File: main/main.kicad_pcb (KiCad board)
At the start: 2 copper layers, 100 x 100 mm, 9 parts

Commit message: started layout to see if practical
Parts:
- removed FID1, FID2, FID3: Fiducial, Fiducial:Fiducial_1mm_Dia_2mm_Outer
- removed G1: DOW, william_logos:dow_logo_10mm
- removed G2: MEC, william_logos:mec_small
- added BT1: RTC battery, william_batteries:Keystone_3034_1x20mm-CoinCell, F.Cu at (117.1, 168.4)
- added C1: 100N, Capacitor_SMD:C_0603_1608Metric, F.Cu at (118.8, 188.2)
- added C10: 100N, Capacitor_SMD:C_0603_1608Metric, F.Cu at (310.5, 116.6)
- added C100: 100N, Capacitor_SMD:C_0603_1608Metric, F.Cu at (310.9, 109.1)
- added C101: 100N, Capacitor_SMD:C_0603_1608Metric, F.Cu at (299.3, 147.0)
- added C102: 100N, Capacitor_SMD:C_0603_1608Metric, F.Cu at (299.3, 142.0)
- added C103: 100N, Capacitor_SMD:C_0603_1608Metric, F.Cu at (319.0, 132.2)
- added C104: 100N, Capacitor_SMD:C_0603_1608Metric, F.Cu at (327.9, 113.4)
- added C105: 100N, Capacitor_SMD:C_0603_1608Metric, F.Cu at (302.7, 171.1)
- added C106: 100N, Capacitor_SMD:C_0603_1608Metric, F.Cu at (273.4, 175.7)
- added C107: 100N, Capacitor_SMD:C_0603_1608Metric, F.Cu at (323.0, 129.7)
- added C108: 100N, Capacitor_SMD:C_0603_1608Metric, F.Cu at (249.4, 175.7)
- added C109: 100N, Capacitor_SMD:C_0603_1608Metric, F.Cu at (323.4, 124.6)
- added C11: 100N, Capacitor_SMD:C_0603_1608Metric, F.Cu at (309.2, 135.8)
- added C110: 100N, Capacitor_SMD:C_0603_1608Metric, F.Cu at (225.3, 175.7)
- added C111: 100N, Capacitor_SMD:C_0603_1608Metric, F.Cu at (233.3, 175.7)
- added C112: 100N, Capacitor_SMD:C_0603_1608Metric, F.Cu at (245.3, 175.7)
- added C113: 100N, Capacitor_SMD:C_0603_1608Metric, F.Cu at (253.4, 175.7)
- added C114: 100N, Capacitor_SMD:C_0603_1608Metric, F.Cu at (261.4, 175.7)
- added C115: 4U7, Capacitor_SMD:C_0603_1608Metric, F.Cu at (325.8, 74.3)
- added C116: 100N, Capacitor_SMD:C_0603_1608Metric, F.Cu at (325.8, 71.8)
- added C117: 100N, Capacitor_SMD:C_0603_1608Metric, F.Cu at (321.8, 74.3)
- added C118: 10N, Capacitor_SMD:C_0603_1608Metric, F.Cu at (317.8, 71.8)
- added C119: 2U2, Capacitor_SMD:C_0603_1608Metric, F.Cu at (326.9, 62.3)
- added C12: 100N, Capacitor_SMD:C_0603_1608Metric, F.Cu at (328.2, 152.0)
- added C120: 100N, Capacitor_SMD:C_0603_1608Metric, F.Cu at (317.8, 74.3)
- added C121: 100N, Capacitor_SMD:C_0603_1608Metric, F.Cu at (326.9, 64.8)
- added C122: 100N, Capacitor_SMD:C_0603_1608Metric, F.Cu at (321.8, 71.8)
- added C123: 100N, Capacitor_SMD:C_0603_1608Metric, F.Cu at (326.9, 67.3)
- added C13: 100N, Capacitor_SMD:C_0603_1608Metric, F.Cu at (313.3, 133.3)
- added C14: 100N, Capacitor_SMD:C_0603_1608Metric, F.Cu at (313.3, 138.3)
- added C15: 100N, Capacitor_SMD:C_0603_1608Metric, F.Cu at (309.2, 130.8)
- added C16: 100N, Capacitor_SMD:C_0603_1608Metric, F.Cu at (302.7, 173.6)
- added C17: 100N, Capacitor_SMD:C_0603_1608Metric, F.Cu at (288.5, 170.6)
- added C18: 100N, Capacitor_SMD:C_0603_1608Metric, F.Cu at (314.9, 109.1)
- added C19: 100N, Capacitor_SMD:C_0603_1608Metric, F.Cu at (269.4, 175.7)
- added C2: 10N, Capacitor_SMD:C_0603_1608Metric, F.Cu at (114.7, 188.2)
- added C20: 100N, Capacitor_SMD:C_0603_1608Metric, F.Cu at (293.7, 175.7)
- added C21: 100N, Capacitor_SMD:C_0603_1608Metric, F.Cu at (221.3, 175.7)
- added C22: 100N, Capacitor_SMD:C_0603_1608Metric, F.Cu at (327.5, 126.0)
- added C23: 100N, Capacitor_SMD:C_0603_1608Metric, F.Cu at (313.3, 130.8)
- added C24: 100N, Capacitor_SMD:C_0603_1608Metric, F.Cu at (323.0, 132.2)
- added C25: 100N, Capacitor_SMD:C_0603_1608Metric, F.Cu at (292.5, 173.1)
- added C26: 100N, Capacitor_SMD:C_0603_1608Metric, F.Cu at (314.5, 116.6)
- added C27: 100N, Capacitor_SMD:C_0603_1608Metric, F.Cu at (327.9, 118.5)
- added C28: 100N, Capacitor_SMD:C_0603_1608Metric, F.Cu at (298.9, 152.1)
- added C29: 100N, Capacitor_SMD:C_0603_1608Metric, F.Cu at (295.3, 142.0)
- added C3: 100N, Capacitor_SMD:C_0603_1608Metric, F.Cu at (106.7, 188.2)
- added C30: 100N, Capacitor_SMD:C_0603_1608Metric, F.Cu at (312.9, 143.3)
- added C31: 100N, Capacitor_SMD:C_0603_1608Metric, F.Cu at (301.5, 168.6)
- added C32: 100N, Capacitor_SMD:C_0603_1608Metric, F.Cu at (308.8, 146.5)
- added C33: 100N, Capacitor_SMD:C_0603_1608Metric, F.Cu at (265.4, 175.7)
- added C34: 100N, Capacitor_SMD:C_0603_1608Metric, F.Cu at (310.5, 119.1)
- added C35: 100N, Capacitor_SMD:C_0603_1608Metric, F.Cu at (323.4, 122.1)
- added C36: 100N, Capacitor_SMD:C_0603_1608Metric, F.Cu at (294.5, 157.1)
- added C37: 100N, Capacitor_SMD:C_0603_1608Metric, F.Cu at (289.7, 175.7)
- added C38: 100N, Capacitor_SMD:C_0603_1608Metric, F.Cu at (324.2, 157.0)
- added C39: 100N, Capacitor_SMD:C_0603_1608Metric, F.Cu at (309.2, 133.3)
- added C4: 10U, Capacitor_SMD:C_0603_1608Metric, F.Cu at (110.7, 188.2)
- added C40: 100N, Capacitor_SMD:C_0603_1608Metric, F.Cu at (319.0, 134.7)
- added C41: 100N, Capacitor_SMD:C_0603_1608Metric, F.Cu at (325.0, 162.0)
- added C42: 100N, Capacitor_SMD:C_0603_1608Metric, F.Cu at (301.9, 163.6)
- added C43: 100N, Capacitor_SMD:C_0603_1608Metric, F.Cu at (314.5, 119.1)
- added C44: 100N, Capacitor_SMD:C_0603_1608Metric, F.Cu at (327.9, 115.9)
- added C45: 100N, Capacitor_SMD:C_0603_1608Metric, F.Cu at (310.5, 121.7)
- added C46: 100N, Capacitor_SMD:C_0603_1608Metric, F.Cu at (288.5, 173.1)
- added C47: 100N, Capacitor_SMD:C_0603_1608Metric, F.Cu at (308.8, 149.0)
- added C48: 100N, Capacitor_SMD:C_0603_1608Metric, F.Cu at (277.4, 175.7)
- added C49: 100N, Capacitor_SMD:C_0603_1608Metric, F.Cu at (327.9, 110.9)
- added C5: 100N, Capacitor_SMD:C_0603_1608Metric, F.Cu at (237.3, 175.7)
- added C50: 100N, Capacitor_SMD:C_0603_1608Metric, F.Cu at (309.2, 138.3)
- added C51: 100N, Capacitor_SMD:C_0603_1608Metric, F.Cu at (328.6, 149.5)
- added C52: 100N, Capacitor_SMD:C_0603_1608Metric, F.Cu at (314.9, 111.6)
- added C53: 100N, Capacitor_SMD:C_0603_1608Metric, F.Cu at (319.0, 129.7)
- added C54: 100N, Capacitor_SMD:C_0603_1608Metric, F.Cu at (328.6, 146.9)
- added C55: 100N, Capacitor_SMD:C_0603_1608Metric, F.Cu at (294.9, 152.1)
- added C56: 100N, Capacitor_SMD:C_0603_1608Metric, F.Cu at (323.4, 127.2)
- added C57: 100N, Capacitor_SMD:C_0603_1608Metric, F.Cu at (295.3, 147.0)
- added C58: 100N, Capacitor_SMD:C_0603_1608Metric, F.Cu at (310.9, 114.1)
- added C59: 100N, Capacitor_SMD:C_0603_1608Metric, F.Cu at (305.5, 168.6)
- added C6: 100N, Capacitor_SMD:C_0603_1608Metric, F.Cu at (229.3, 175.7)
- added C60: 100N, Capacitor_SMD:C_0603_1608Metric, F.Cu at (293.7, 178.2)
- added C61: 100N, Capacitor_SMD:C_0603_1608Metric, F.Cu at (308.8, 144.0)
- added C62: 100N, Capacitor_SMD:C_0603_1608Metric, F.Cu at (309.2, 140.8)
- added C63: 100N, Capacitor_SMD:C_0603_1608Metric, F.Cu at (324.2, 154.5)
- added C64: 100N, Capacitor_SMD:C_0603_1608Metric, F.Cu at (313.3, 135.8)
- added C65: 100N, Capacitor_SMD:C_0603_1608Metric, F.Cu at (294.9, 149.5)
- added C66: 100N, Capacitor_SMD:C_0603_1608Metric, F.Cu at (324.2, 152.0)
- added C67: 100N, Capacitor_SMD:C_0603_1608Metric, F.Cu at (327.9, 123.5)
- added C68: 100N, Capacitor_SMD:C_0603_1608Metric, F.Cu at (305.9, 166.1)
- added C69: 100N, Capacitor_SMD:C_0603_1608Metric, F.Cu at (299.3, 144.5)
- added C7: 100N, Capacitor_SMD:C_0603_1608Metric, F.Cu at (301.9, 161.1)
- added C70: 100N, Capacitor_SMD:C_0603_1608Metric, F.Cu at (319.0, 139.7)
- added C71: 100N, Capacitor_SMD:C_0603_1608Metric, F.Cu at (327.5, 131.0)
- added C72: 100N, Capacitor_SMD:C_0603_1608Metric, F.Cu at (312.9, 145.8)
- added C73: 100N, Capacitor_SMD:C_0603_1608Metric, F.Cu at (305.9, 161.1)
- added C74: 100N, Capacitor_SMD:C_0603_1608Metric, F.Cu at (325.0, 159.5)
- added C75: 100N, Capacitor_SMD:C_0603_1608Metric, F.Cu at (324.6, 144.4)
- added C76: 100N, Capacitor_SMD:C_0603_1608Metric, F.Cu at (328.2, 157.0)
- added C77: 100N, Capacitor_SMD:C_0603_1608Metric, F.Cu at (292.5, 170.6)
- added C78: 100N, Capacitor_SMD:C_0603_1608Metric, F.Cu at (298.9, 149.5)
- added C79: 100N, Capacitor_SMD:C_0603_1608Metric, F.Cu at (319.4, 122.1)
- added C8: 100N, Capacitor_SMD:C_0603_1608Metric, F.Cu at (257.4, 175.7)
- added C80: 100N, Capacitor_SMD:C_0603_1608Metric, F.Cu at (310.9, 111.6)
- added C81: 100N, Capacitor_SMD:C_0603_1608Metric, F.Cu at (294.9, 154.6)
- added C82: 100N, Capacitor_SMD:C_0603_1608Metric, F.Cu at (327.9, 121.0)
- added C83: 100N, Capacitor_SMD:C_0603_1608Metric, F.Cu at (328.2, 154.5)
- added C84: 100N, Capacitor_SMD:C_0603_1608Metric, F.Cu at (319.4, 127.2)
- added C85: 100N, Capacitor_SMD:C_0603_1608Metric, F.Cu at (306.7, 171.1)
- added C86: 100N, Capacitor_SMD:C_0603_1608Metric, F.Cu at (289.7, 178.2)
- added C87: 100N, Capacitor_SMD:C_0603_1608Metric, F.Cu at (327.5, 128.5)
- added C88: 100N, Capacitor_SMD:C_0603_1608Metric, F.Cu at (328.6, 144.4)
- added C89: 100N, Capacitor_SMD:C_0603_1608Metric, F.Cu at (314.9, 114.1)
- added C9: 100N, Capacitor_SMD:C_0603_1608Metric, F.Cu at (241.3, 175.7)
- added C90: 100N, Capacitor_SMD:C_0603_1608Metric, F.Cu at (295.3, 144.5)
- added C91: 100N, Capacitor_SMD:C_0603_1608Metric, F.Cu at (305.9, 163.6)
- added C92: 100N, Capacitor_SMD:C_0603_1608Metric, F.Cu at (324.6, 149.5)
- added C93: 100N, Capacitor_SMD:C_0603_1608Metric, F.Cu at (323.0, 134.7)
- added C94: 100N, Capacitor_SMD:C_0603_1608Metric, F.Cu at (319.4, 124.6)
- added C95: 100N, Capacitor_SMD:C_0603_1608Metric, F.Cu at (319.0, 137.2)
- added C96: 100N, Capacitor_SMD:C_0603_1608Metric, F.Cu at (324.6, 146.9)
- added C97: 100N, Capacitor_SMD:C_0603_1608Metric, F.Cu at (313.3, 140.8)
- added C98: 100N, Capacitor_SMD:C_0603_1608Metric, F.Cu at (301.9, 166.1)
- added C99: 100N, Capacitor_SMD:C_0603_1608Metric, F.Cu at (306.7, 173.6)
- added D1: WS2813-Mini, william_led:WS2813-Mini-3.5mm_x_3.5mm, F.Cu at (8.96, 5.14)
- added D10: WS2813-Mini, william_led:WS2813-Mini-3.5mm_x_3.5mm, F.Cu at (8.58, 85.2)
- added D100: WS2813-Mini, william_led:WS2813-Mini-3.5mm_x_3.5mm, F.Cu at (82.5, 95.3)
- added D101: WS2813-Mini, william_led:WS2813-Mini-3.5mm_x_3.5mm, F.Cu at (85.7, 5.14)
- added D102: WS2813-Mini, william_led:WS2813-Mini-3.5mm_x_3.5mm, F.Cu at (94.0, 12.8)
- added D103: WS2813-Mini, william_led:WS2813-Mini-3.5mm_x_3.5mm, F.Cu at (93.0, 23.6)
- added D104: WS2813-Mini, william_led:WS2813-Mini-3.5mm_x_3.5mm, F.Cu at (94.4, 31.6)
- added D105: WS2813-Mini, william_led:WS2813-Mini-3.5mm_x_3.5mm, F.Cu at (93.4, 41.0)
- added D106: WS2813-Mini, william_led:WS2813-Mini-3.5mm_x_3.5mm, F.Cu at (92.8, 48.2)
- added D107: WS2813-Mini, william_led:WS2813-Mini-3.5mm_x_3.5mm, F.Cu at (93.3, 59.6)
- added D108: WS2813-Mini, william_led:WS2813-Mini-3.5mm_x_3.5mm, F.Cu at (93.7, 68.5)
- added D109: WS2813-Mini, william_led:WS2813-Mini-3.5mm_x_3.5mm, F.Cu at (90.5, 86.0)
- added D11: WS2813-Mini, william_led:WS2813-Mini-3.5mm_x_3.5mm, F.Cu at (16.6, 5.14)
- added D110: WS2813-Mini, william_led:WS2813-Mini-3.5mm_x_3.5mm, F.Cu at (90.7, 95.1)
- added D12: WS2813-Mini, william_led:WS2813-Mini-3.5mm_x_3.5mm, F.Cu at (17.8, 12.4)
- added D13: WS2813-Mini, william_led:WS2813-Mini-3.5mm_x_3.5mm, F.Cu at (16.6, 21.9)
- added D14: WS2813-Mini, william_led:WS2813-Mini-3.5mm_x_3.5mm, F.Cu at (16.5, 31.4)
- added D15: WS2813-Mini, william_led:WS2813-Mini-3.5mm_x_3.5mm, F.Cu at (16.4, 39.1)
- added D16: WS2813-Mini, william_led:WS2813-Mini-3.5mm_x_3.5mm, F.Cu at (17.3, 47.1)
- added D17: WS2813-Mini, william_led:WS2813-Mini-3.5mm_x_3.5mm, F.Cu at (17.7, 55.8)
- added D18: WS2813-Mini, william_led:WS2813-Mini-3.5mm_x_3.5mm, F.Cu at (18.2, 74.4)
- added D19: WS2813-Mini, william_led:WS2813-Mini-3.5mm_x_3.5mm, F.Cu at (15.4, 85.7)
- added D2: WS2813-Mini, william_led:WS2813-Mini-3.5mm_x_3.5mm, F.Cu at (8.96, 12.5)
- added D20: WS2813-Mini, william_led:WS2813-Mini-3.5mm_x_3.5mm, F.Cu at (15.6, 95.2)
- added D21: WS2813-Mini, william_led:WS2813-Mini-3.5mm_x_3.5mm, F.Cu at (24.3, 5.14)
- added D22: WS2813-Mini, william_led:WS2813-Mini-3.5mm_x_3.5mm, F.Cu at (26.1, 12.1)
- added D23: WS2813-Mini, william_led:WS2813-Mini-3.5mm_x_3.5mm, F.Cu at (24.8, 22.2)
- added D24: WS2813-Mini, william_led:WS2813-Mini-3.5mm_x_3.5mm, F.Cu at (25.2, 31.4)
- added D25: WS2813-Mini, william_led:WS2813-Mini-3.5mm_x_3.5mm, F.Cu at (26.2, 39.1)
- added D26: WS2813-Mini, william_led:WS2813-Mini-3.5mm_x_3.5mm, F.Cu at (27.1, 46.8)
- added D27: WS2813-Mini, william_led:WS2813-Mini-3.5mm_x_3.5mm, F.Cu at (26.5, 55.6)
- added D28: WS2813-Mini, william_led:WS2813-Mini-3.5mm_x_3.5mm, F.Cu at (27.1, 74.4)
- added D29: WS2813-Mini, william_led:WS2813-Mini-3.5mm_x_3.5mm, F.Cu at (24.3, 85.4)
- added D3: WS2813-Mini, william_led:WS2813-Mini-3.5mm_x_3.5mm, F.Cu at (8.96, 22.0)
- added D30: WS2813-Mini, william_led:WS2813-Mini-3.5mm_x_3.5mm, F.Cu at (26.5, 94.9)
- added D31: WS2813-Mini, william_led:WS2813-Mini-3.5mm_x_3.5mm, F.Cu at (32.0, 5.14)
- added D32: WS2813-Mini, william_led:WS2813-Mini-3.5mm_x_3.5mm, F.Cu at (34.9, 12.1)
- added D33: WS2813-Mini, william_led:WS2813-Mini-3.5mm_x_3.5mm, F.Cu at (36.8, 22.4)
- added D34: WS2813-Mini, william_led:WS2813-Mini-3.5mm_x_3.5mm, F.Cu at (33.8, 31.4)
- added D35: WS2813-Mini, william_led:WS2813-Mini-3.5mm_x_3.5mm, F.Cu at (36.0, 40.1)
- added D36: WS2813-Mini, william_led:WS2813-Mini-3.5mm_x_3.5mm, F.Cu at (35.9, 46.9)
- added D37: WS2813-Mini, william_led:WS2813-Mini-3.5mm_x_3.5mm, F.Cu at (34.2, 56.1)
- added D38: WS2813-Mini, william_led:WS2813-Mini-3.5mm_x_3.5mm, F.Cu at (36.3, 74.9)
- added D39: WS2813-Mini, william_led:WS2813-Mini-3.5mm_x_3.5mm, F.Cu at (34.5, 85.3)
- added D4: WS2813-Mini, william_led:WS2813-Mini-3.5mm_x_3.5mm, F.Cu at (8.96, 31.4)
- added D40: WS2813-Mini, william_led:WS2813-Mini-3.5mm_x_3.5mm, F.Cu at (34.4, 95.3)
- added D41: WS2813-Mini, william_led:WS2813-Mini-3.5mm_x_3.5mm, F.Cu at (39.6, 5.14)
- added D42: WS2813-Mini, william_led:WS2813-Mini-3.5mm_x_3.5mm, F.Cu at (46.9, 11.9)
- added D43: WS2813-Mini, william_led:WS2813-Mini-3.5mm_x_3.5mm, F.Cu at (45.5, 22.4)
- added D44: WS2813-Mini, william_led:WS2813-Mini-3.5mm_x_3.5mm, F.Cu at (42.5, 31.4)
- added D45: WS2813-Mini, william_led:WS2813-Mini-3.5mm_x_3.5mm, F.Cu at (44.8, 39.2)
- added D46: WS2813-Mini, william_led:WS2813-Mini-3.5mm_x_3.5mm, F.Cu at (45.3, 45.5)
- added D47: WS2813-Mini, william_led:WS2813-Mini-3.5mm_x_3.5mm, F.Cu at (43.0, 58.0)
- added D48: WS2813-Mini, william_led:WS2813-Mini-3.5mm_x_3.5mm, F.Cu at (45.4, 75.1)
- added D49: WS2813-Mini, william_led:WS2813-Mini-3.5mm_x_3.5mm, F.Cu at (45.5, 85.0)
- added D5: WS2813-Mini, william_led:WS2813-Mini-3.5mm_x_3.5mm, F.Cu at (8.96, 38.9)
- added D50: WS2813-Mini, william_led:WS2813-Mini-3.5mm_x_3.5mm, F.Cu at (43.2, 95.4)
- added D51: WS2813-Mini, william_led:WS2813-Mini-3.5mm_x_3.5mm, F.Cu at (47.3, 5.14)
- added D52: WS2813-Mini, william_led:WS2813-Mini-3.5mm_x_3.5mm, F.Cu at (57.3, 11.4)
- added D53: WS2813-Mini, william_led:WS2813-Mini-3.5mm_x_3.5mm, F.Cu at (52.8, 22.4)
- added D54: WS2813-Mini, william_led:WS2813-Mini-3.5mm_x_3.5mm, F.Cu at (51.2, 31.4)
- added D55: WS2813-Mini, william_led:WS2813-Mini-3.5mm_x_3.5mm, F.Cu at (53.0, 38.2)
- added D56: WS2813-Mini, william_led:WS2813-Mini-3.5mm_x_3.5mm, F.Cu at (53.8, 45.0)
- added D57: WS2813-Mini, william_led:WS2813-Mini-3.5mm_x_3.5mm, F.Cu at (50.7, 58.2)
- added D58: WS2813-Mini, william_led:WS2813-Mini-3.5mm_x_3.5mm, F.Cu at (54.0, 75.1)
- added D59: WS2813-Mini, william_led:WS2813-Mini-3.5mm_x_3.5mm, F.Cu at (53.7, 84.9)
- added D6: WS2813-Mini, william_led:WS2813-Mini-3.5mm_x_3.5mm, F.Cu at (8.96, 47.3)
- added D60: WS2813-Mini, william_led:WS2813-Mini-3.5mm_x_3.5mm, F.Cu at (51.4, 95.7)
- added D61: WS2813-Mini, william_led:WS2813-Mini-3.5mm_x_3.5mm, F.Cu at (55.0, 5.14)
- added D62: WS2813-Mini, william_led:WS2813-Mini-3.5mm_x_3.5mm, F.Cu at (66.4, 11.5)
- added D63: WS2813-Mini, william_led:WS2813-Mini-3.5mm_x_3.5mm, F.Cu at (59.5, 23.4)
- added D64: WS2813-Mini, william_led:WS2813-Mini-3.5mm_x_3.5mm, F.Cu at (59.9, 31.4)
- added D65: WS2813-Mini, william_led:WS2813-Mini-3.5mm_x_3.5mm, F.Cu at (62.6, 39.1)
- added D66: WS2813-Mini, william_led:WS2813-Mini-3.5mm_x_3.5mm, F.Cu at (62.9, 47.7)
- added D67: WS2813-Mini, william_led:WS2813-Mini-3.5mm_x_3.5mm, F.Cu at (58.6, 58.0)
- added D68: WS2813-Mini, william_led:WS2813-Mini-3.5mm_x_3.5mm, F.Cu at (62.8, 72.6)
- added D69: WS2813-Mini, william_led:WS2813-Mini-3.5mm_x_3.5mm, F.Cu at (59.9, 84.5)
- added D7: WS2813-Mini, william_led:WS2813-Mini-3.5mm_x_3.5mm, F.Cu at (8.96, 55.1)
- added D70: WS2813-Mini, william_led:WS2813-Mini-3.5mm_x_3.5mm, F.Cu at (59.6, 95.8)
- added D71: WS2813-Mini, william_led:WS2813-Mini-3.5mm_x_3.5mm, F.Cu at (62.7, 5.14)
- added D72: WS2813-Mini, william_led:WS2813-Mini-3.5mm_x_3.5mm, F.Cu at (73.1, 11.9)
- added D73: WS2813-Mini, william_led:WS2813-Mini-3.5mm_x_3.5mm, F.Cu at (67.8, 23.3)
- added D74: WS2813-Mini, william_led:WS2813-Mini-3.5mm_x_3.5mm, F.Cu at (68.5, 31.4)
- added D75: WS2813-Mini, william_led:WS2813-Mini-3.5mm_x_3.5mm, F.Cu at (69.0, 38.8)
- added D76: WS2813-Mini, william_led:WS2813-Mini-3.5mm_x_3.5mm, F.Cu at (70.8, 45.0)
- added D77: WS2813-Mini, william_led:WS2813-Mini-3.5mm_x_3.5mm, F.Cu at (66.9, 58.4)
- added D78: WS2813-Mini, william_led:WS2813-Mini-3.5mm_x_3.5mm, F.Cu at (72.8, 67.9)
- added D79: WS2813-Mini, william_led:WS2813-Mini-3.5mm_x_3.5mm, F.Cu at (66.5, 85.5)
- added D8: WS2813-Mini, william_led:WS2813-Mini-3.5mm_x_3.5mm, F.Cu at (8.58, 63.1)
- added D80: WS2813-Mini, william_led:WS2813-Mini-3.5mm_x_3.5mm, F.Cu at (67.8, 95.4)
- added D81: WS2813-Mini, william_led:WS2813-Mini-3.5mm_x_3.5mm, F.Cu at (70.3, 5.14)
- added D82: WS2813-Mini, william_led:WS2813-Mini-3.5mm_x_3.5mm, F.Cu at (78.3, 12.6)
- added D83: WS2813-Mini, william_led:WS2813-Mini-3.5mm_x_3.5mm, F.Cu at (75.0, 23.7)
- added D84: WS2813-Mini, william_led:WS2813-Mini-3.5mm_x_3.5mm, F.Cu at (77.2, 31.4)
- added D85: WS2813-Mini, william_led:WS2813-Mini-3.5mm_x_3.5mm, F.Cu at (74.9, 39.9)
- added D86: WS2813-Mini, william_led:WS2813-Mini-3.5mm_x_3.5mm, F.Cu at (76.3, 48.4)
- added D87: WS2813-Mini, william_led:WS2813-Mini-3.5mm_x_3.5mm, F.Cu at (75.3, 58.5)
- added D88: WS2813-Mini, william_led:WS2813-Mini-3.5mm_x_3.5mm, F.Cu at (77.8, 68.3)
- added D89: WS2813-Mini, william_led:WS2813-Mini-3.5mm_x_3.5mm, F.Cu at (74.0, 85.4)
- added D9: WS2813-Mini, william_led:WS2813-Mini-3.5mm_x_3.5mm, F.Cu at (8.58, 75.9)
- added D90: WS2813-Mini, william_led:WS2813-Mini-3.5mm_x_3.5mm, F.Cu at (74.2, 94.9)
- added D91: WS2813-Mini, william_led:WS2813-Mini-3.5mm_x_3.5mm, F.Cu at (78.0, 5.14)
- added D92: WS2813-Mini, william_led:WS2813-Mini-3.5mm_x_3.5mm, F.Cu at (86.8, 12.8)
- added D93: WS2813-Mini, william_led:WS2813-Mini-3.5mm_x_3.5mm, F.Cu at (83.3, 23.2)
- added D94: WS2813-Mini, william_led:WS2813-Mini-3.5mm_x_3.5mm, F.Cu at (85.5, 31.3)
- added D95: WS2813-Mini, william_led:WS2813-Mini-3.5mm_x_3.5mm, F.Cu at (83.0, 40.8)
- added D96: WS2813-Mini, william_led:WS2813-Mini-3.5mm_x_3.5mm, F.Cu at (83.3, 48.1)
- added D97: WS2813-Mini, william_led:WS2813-Mini-3.5mm_x_3.5mm, F.Cu at (83.8, 58.7)
- added D98: WS2813-Mini, william_led:WS2813-Mini-3.5mm_x_3.5mm, F.Cu at (86.4, 67.5)
- added D99: WS2813-Mini, william_led:WS2813-Mini-3.5mm_x_3.5mm, F.Cu at (81.5, 85.8)
- added J1: USB_B_Micro, Connector_USB:USB_Micro-B_GCT_USB3076-30-A, F.Cu at (156.8, 178.8)
- added J2: TC2030-IDC, Connector:Tag-Connect_TC2030-IDC-FP_2x03_P1.27mm_Vertical, F.Cu at (320.6, 65.8)
- added SW1: SW_SPST, Button_Switch_SMD:SW_Push_1P1T_NO_6x6mm_H9.5mm, F.Cu at (135.0, 176.3)
- added SW2: SW_SPST, Button_Switch_SMD:SW_Push_1P1T_NO_6x6mm_H9.5mm, F.Cu at (146.1, 161.1)
- added SW3: SW_SPST, Button_Switch_SMD:SW_Push_1P1T_NO_6x6mm_H9.5mm, F.Cu at (135.0, 168.7)
- added SW4: SW_SPST, Button_Switch_SMD:SW_Push_1P1T_NO_6x6mm_H9.5mm, F.Cu at (121.3, 183.2)
- added SW5: SW_SPST, Button_Switch_SMD:SW_Push_1P1T_NO_6x6mm_H9.5mm, F.Cu at (135.0, 161.1)
- added SW6: SW_SPST, Button_Switch_SMD:SW_Push_1P1T_NO_6x6mm_H9.5mm, F.Cu at (110.2, 183.2)
- added U1: AP1117-33, Package_TO_SOT_SMD:SOT-223-3_TabPin2, F.Cu at (156.5, 161.5)
- added U2: STM32F401RBTx, Package_QFP:LQFP-64_10x10mm_P0.5mm, F.Cu at (308.6, 68.3)
- moved H1 264.3 mm to (363.8, 86.0)
- moved H2 264.0 mm to (363.8, 93.6)
- moved H4 183.4 mm to (371.3, 93.6)
- moved H3 183.0 mm to (371.3, 86.0)
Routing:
- net Net-(D1-Pad3): track 0.00 -> 8.34 mm
- removed copper zone on B.Cu, net (none)
- removed copper zone on F.Cu, net (none)
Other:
- outline, holes or cut-outs redrawn
- board text removed: "PROJECT_NAME v0.0.0 batch 0 1/1/2000"

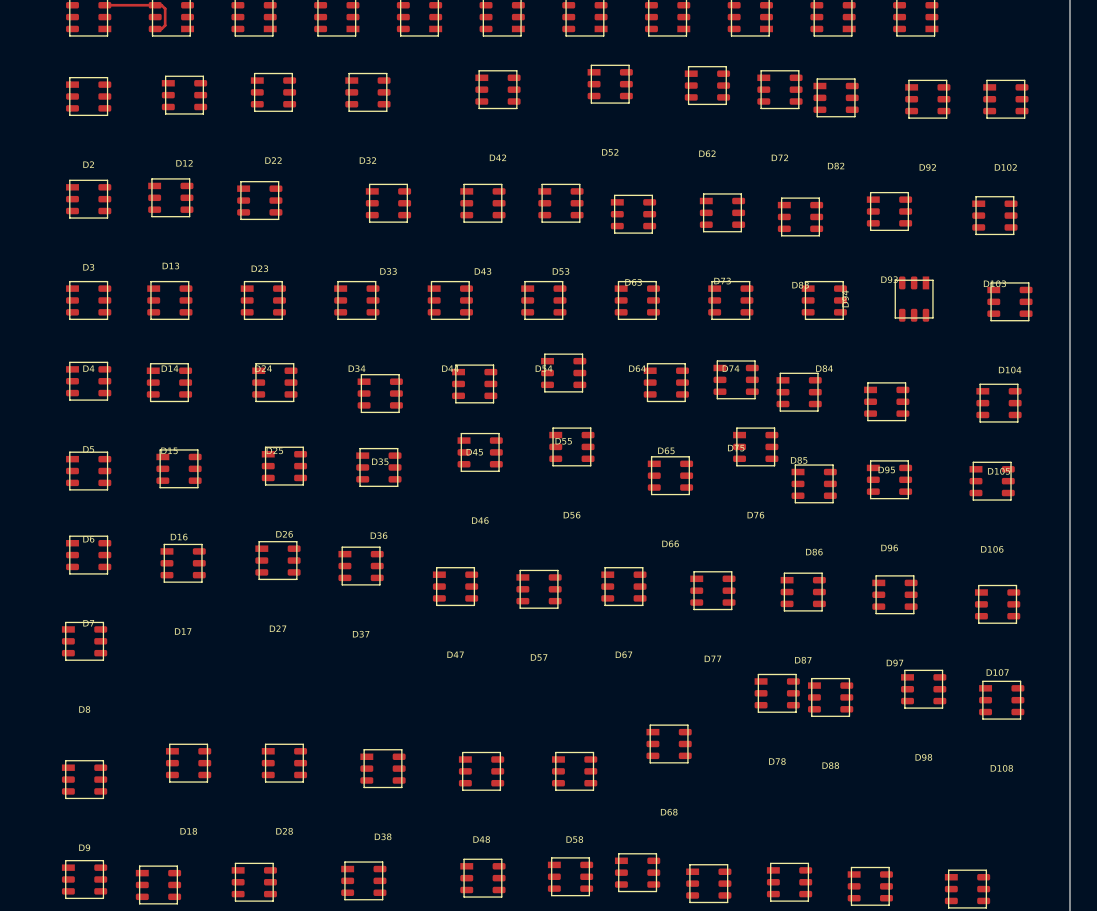
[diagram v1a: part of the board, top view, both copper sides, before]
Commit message: squaring up array to see what spacing is reasonable
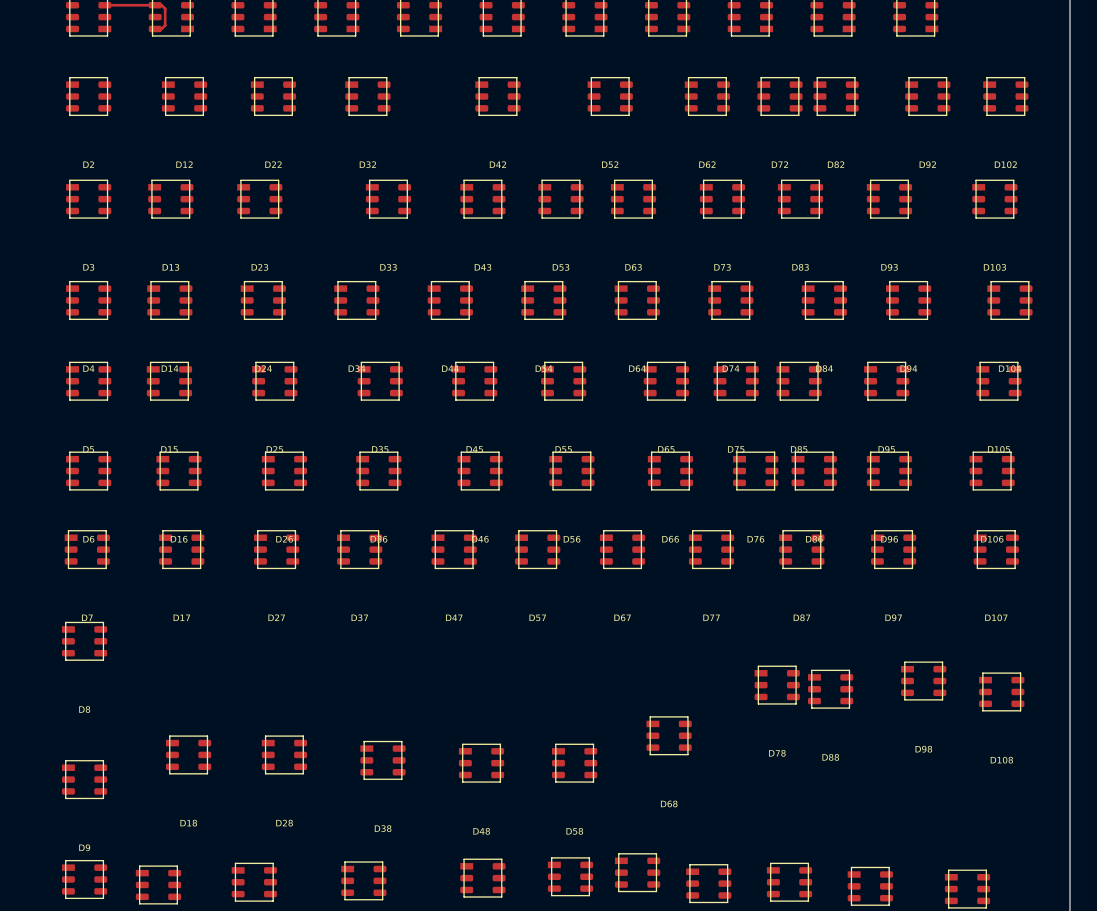
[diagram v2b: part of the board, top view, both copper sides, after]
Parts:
- moved D107 5.08 mm to (93.2, 54.5)
- moved D97 4.19 mm to (83.6, 54.5)
- moved D87 3.94 mm to (75.1, 54.5)
- moved D77 3.81 mm to (66.7, 54.5)
- moved D57 3.69 mm to (50.6, 54.5)
- moved D47 3.43 mm to (42.9, 54.5)
- moved D67 3.43 mm to (58.5, 54.5)
- moved D56 2.23 mm to (53.8, 47.3)
- moved D76 2.23 mm to (70.8, 47.3)
- moved D105 2.03 mm to (93.4, 38.9)
- moved D95 1.91 mm to (83.0, 38.9)
- moved D46 1.73 mm to (45.3, 47.3)
- moved D83 1.65 mm to (75.0, 22.0)
- moved D37 1.53 mm to (34.1, 54.5)
- moved D103 1.52 mm to (93.0, 22.0)
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
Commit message: most components
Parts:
- removed C120: 100N, Capacitor_SMD:C_0603_1608Metric
- added C124: 21P, Capacitor_SMD:C_0402_1005Metric, F.Cu at (7.25, 15.5)
- added Y1: Crystal, Crystal:Crystal_SMD_3215-2Pin_3.2x1.5mm, F.Cu at (6.00, 13.2)
- BT1: moved to B.Cu
- C1, C10, C100, C101, C102, C103, C104, C105, C106, C107, C108, C109, C11, C110, C111, C112, C113, C114, C115, C116, C117, C118, C119, C12, C121, C122, C13, C14, C15, C16, C17, C18, C19, C20, C21, C22, C23, C24, C25, C26, C27, C28, C29, C3, C30, C31, C32, C33, C34, C35, C36, C37, C38, C39, C4, C40, C41, C42, C43, C44, C45, C46, C47, C48, C49, C5, C50, C51, C52, C53, C54, C55, C56, C57, C58, C59, C6, C60, C61, C62, C63, C64, C65, C66, C67, C68, C69, C7, C70, C71, C72, C73, C74, C75, C76, C77, C78, C79, C8, C80, C81, C82, C83, C84, C85, C86, C87, C88, C89, C9, C90, C91, C92, C93, C94, C95, C96, C97, C98, C99: footprint Capacitor_SMD:C_0603_1608Metric -> Capacitor_SMD:C_0402_1005Metric
- C123: value 100N -> 21P; footprint Capacitor_SMD:C_0603_1608Metric -> Capacitor_SMD:C_0402_1005Metric
- C2: value 10N -> 100N; footprint Capacitor_SMD:C_0603_1608Metric -> Capacitor_SMD:C_0402_1005Metric
- H1, H2, H3, H4: footprint MountingHole:MountingHole_3mm_Pad_Via -> MountingHole:MountingHole_2.1mm
- J2: value TC2030-IDC -> SWD; footprint Connector:Tag-Connect_TC2030-IDC-FP_2x03_P1.27mm_Vertical -> Connector_PinHeader_2.54mm:PinHeader_1x06_P2.54mm_Vertical
- SW1, SW2, SW3, SW4, SW5, SW6: footprint Button_Switch_SMD:SW_Push_1P1T_NO_6x6mm_H9.5mm -> william_switch:KAN4562-0501C
- U2: value STM32F401RBTx -> STM32F401CBUx; footprint Package_QFP:LQFP-64_10x10mm_P0.5mm -> Package_DFN_QFN:QFN-48-1EP_7x7mm_P0.5mm_EP5.6x5.6mm
- moved H2 358.8 mm to (5.00, 95.0)
- moved H1 357.0 mm to (15.0, 10.0)
- moved C123 326.2 mm to (4.75, 15.5), turned to 270 degrees
- moved C117 326.1 mm to (3.75, 2.25), turned to 90 degrees
- moved C122 324.6 mm to (4.75, 2.25), turned to 90 degrees
- moved C115 322.1 mm to (12.0, 1.75)
- moved C116 321.3 mm to (12.0, 2.75)
- moved C121 321.0 mm to (10.0, 13.2)
- moved C119 319.3 mm to (12.5, 6.50), turned to 270 degrees
- moved C118 313.9 mm to (9.00, 15.5), turned to 270 degrees
- moved U2 306.9 mm to (7.75, 7.50), turned to 90 degrees
- moved J2 298.6 mm to (28.8, 2.50), turned to 270 degrees
- moved C37 292.8 mm to (123.8, -65.6)
- moved C86 292.8 mm to (123.8, -63.1)
- moved C17 292.8 mm to (122.6, -70.7)
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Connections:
- C123 pad 1: +3V3 -> /mic/OSC_IN
- C2 pad 1: +5V -> +3V3
- J2 pad 2: (no net) -> /mic/SWCLK
- J2 pad 3: /mic/~RST -> GND
- J2 pad 4: (no net) -> /mic/SWDIO
- J2 pad 5: GND -> /mic/~RST
- U2 pad 12: GND -> (no net)
- U2 pad 13: +3V3 -> /LEDs/DIN
- U2 pad 14: /SWITCH0 -> (no net)
- U2 pad 15: /SWITCH1 -> (no net)
- U2 pad 16: /SWITCH2 -> (no net)
- U2 pad 17: /SWITCH3 -> (no net)
- U2 pad 18: GND -> (no net)
- U2 pad 19: +3V3 -> (no net)
- U2 pad 20: /SWITCH4 -> (no net)
- U2 pad 21: /SWITCH5 -> (no net)
- U2 pad 22: (no net) -> /mic/VCAP1
- U2 pad 23: (no net) -> GND
- U2 pad 24: (no net) -> +3V3
- U2 pad 3: (no net) -> /mic/OSC_IN
- U2 pad 30: /mic/VCAP1 -> (no net)
- U2 pad 31: GND -> (no net)
- U2 pad 32: +3V3 -> (no net)
- U2 pad 34: (no net) -> /mic/SWDIO
- U2 pad 35: (no net) -> GND
- U2 pad 36: (no net) -> +3V3
- U2 pad 37: (no net) -> /mic/SWCLK
- U2 pad 39: (no net) -> /mic/SWO
- U2 pad 4: (no net) -> /mic/OSC_OUT
- U2 pad 40: (no net) -> /SWITCH0
- U2 pad 41: (no net) -> /SWITCH1
- U2 pad 42: (no net) -> /SWITCH2
- U2 pad 43: (no net) -> /SWITCH3
- U2 pad 44: (no net) -> GND
- U2 pad 45: (no net) -> /SWITCH4
- U2 pad 46: /LEDs/DIN -> /SWITCH5
- U2 pad 49: (no net) -> GND
- U2 pad 8: (no net) -> GND
- U2 pad 9: (no net) -> +3V3
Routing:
- net Net-(D1-Pad3): track 8.34 -> 0.00 mm
- net Net-(D11-Pad3): track 0.00 -> 7.62 mm
- net GND: track 0.00 -> 1.25 mm, vias 0 -> 1
- added copper zone on F.Cu, net +5V
- added copper zone on B.Cu, net GND

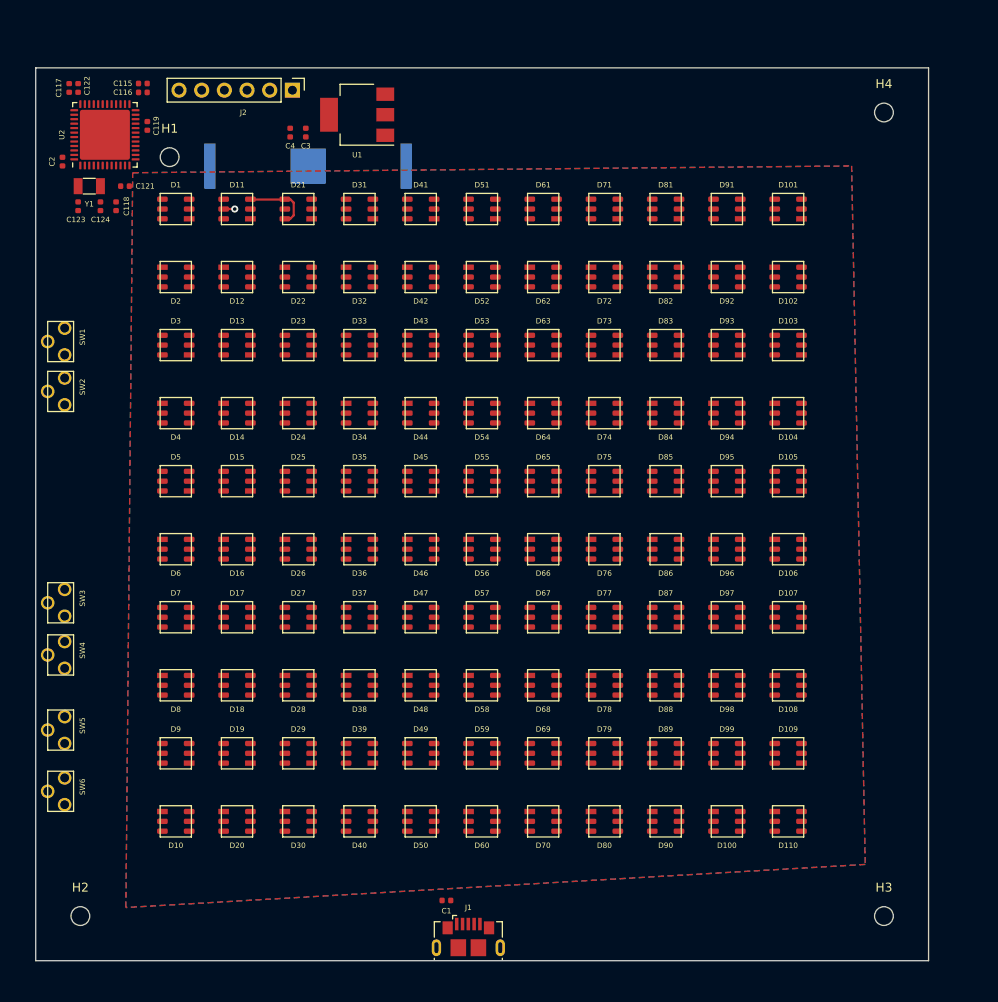
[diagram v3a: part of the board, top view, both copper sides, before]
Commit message: started layout.  Trying to figure out star power topology into MCU
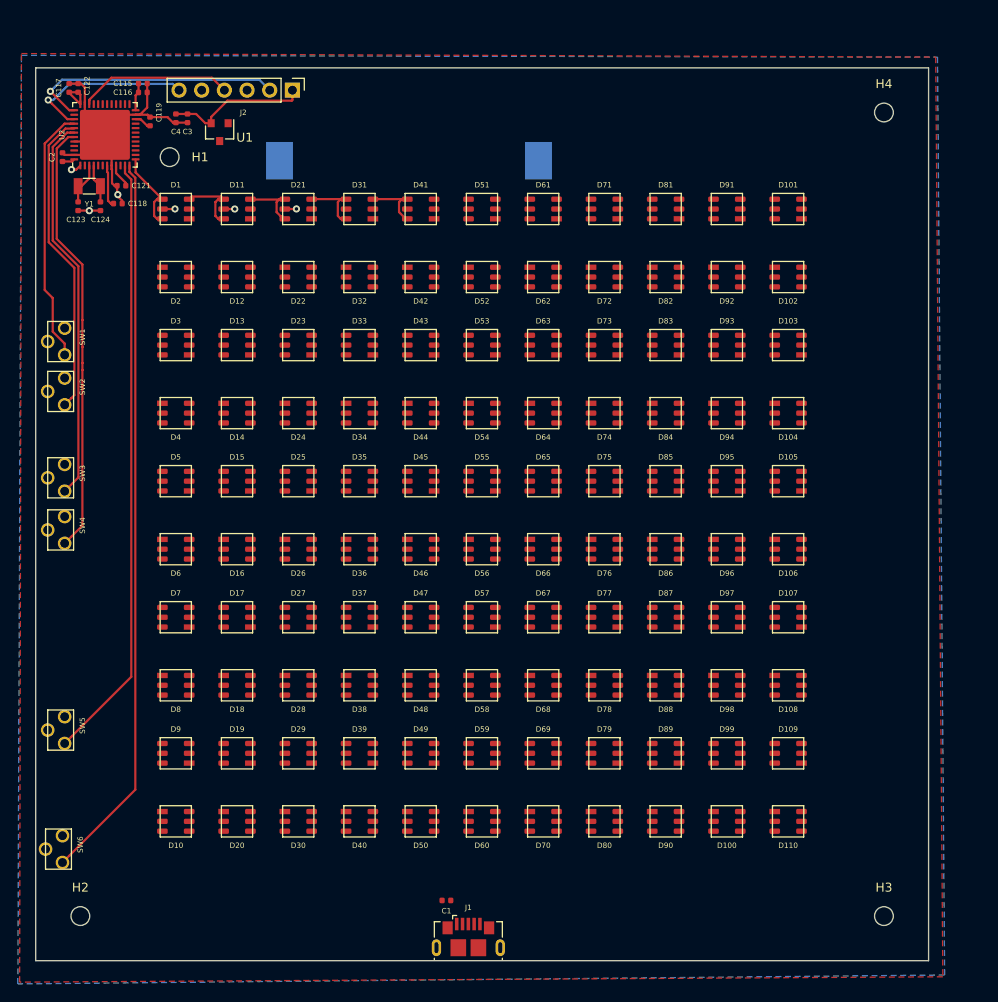
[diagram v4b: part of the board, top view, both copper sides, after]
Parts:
- BT1: value RTC battery -> CR2032-BS-6-1; footprint william_batteries:Keystone_3034_1x20mm-CoinCell -> william_batteries:CR2032-BS-6-1
- U1: value AP1117-33 -> LN6206P332MR-G; footprint Package_TO_SOT_SMD:SOT-223-3_TabPin2 -> Package_TO_SOT_SMD:SOT-23
- moved U1 15.5 mm to (20.6, 7.20), turned to 270 degrees
- moved SW4 14.0 mm to (3.24, 50.3)
- moved SW3 14.0 mm to (3.24, 44.4)
- moved C3 13.3 mm to (17.0, 5.65)
- moved C4 12.9 mm to (15.7, 5.65)
- moved BT1 11.3 mm to (41.8, 10.4), turned to 270 degrees
- moved SW6 6.48 mm to (3.00, 86.0)
- moved C119 0.58 mm to (12.8, 6.00), turned to 90 degrees
- moved C2 0.50 mm to (3.00, 10.0)
- moved C121 0.40 mm to (9.60, 13.2), turned to 180 degrees
- moved C118 0.36 mm to (9.20, 15.2), turned to 0 degrees
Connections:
- U2 pad 11: (no net) -> /SWITCH4
- U2 pad 12: (no net) -> /SWITCH5
- U2 pad 45: /SWITCH4 -> (no net)
- U2 pad 46: /SWITCH5 -> (no net)
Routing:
- net /SWITCH5: track 0.00 -> 81.7 mm
- net /SWITCH4: track 0.00 -> 68.1 mm
- net /SWITCH3: track 0.00 -> 48.7 mm
- net GND: track 1.25 -> 47.9 mm, vias 1 -> 5
- net /SWITCH2: track 0.00 -> 43.5 mm
- net /SWITCH1: track 0.00 -> 34.3 mm
- net /mic/SWCLK: track 0.00 -> 29.1 mm, vias 0 -> 1
- net /SWITCH0: track 0.00 -> 28.8 mm
- net +3V3: track 0.00 -> 27.6 mm
- net /mic/SWO: track 0.00 -> 19.5 mm, vias 0 -> 1
- net /mic/SWDIO: track 0.00 -> 17.2 mm
- net /LEDs/DIN: track 0.00 -> 9.37 mm
- net Net-(D1-Pad3): track 0.00 -> 7.78 mm
- net Net-(D21-Pad3): track 0.00 -> 7.54 mm
- net Net-(D31-Pad3): track 0.00 -> 7.28 mm
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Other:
- board text added: "- +"
- board text added: "BRIGHTNESS (HOLD)"
- board text added: "HOUR"
- board text added: "MIN"
- board text added: "MODE"
